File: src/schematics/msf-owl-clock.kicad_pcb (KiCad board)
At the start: 4 copper layers, 130.1 x 183.6 mm, 448 parts, among them Q101 NX6008NBKW, Q301 NX6008NBKW, Q501 NX6008NBKW, Q502 NX6008NBKW, Q503 NX6008NBKW, Q504 NX6008NBKW, Q505 NX6008NBKW, Q601 NX6008NBKW, Q602 BC847BS, Q603 BC847BS, U001 BC805M, U002 TSOP75338TT, U101 MP5016HGQH, U102 BQ24392RSER, U103 FUSB302BMPX, U104 TPS628512DRLR, U201 TPS7A2040PDQNR, U202 TPS7A2036PDBVR, U203 MCP6499, U204 MCP6499, U205 74HC595BQ, U206 TMUX1511RSV, U207 TMUX1511RSV, U301 PIC32CX1025SG41100-I/E5X, U302 AP22653AW6, U401 AP22653AW6, U402 MCP6486U, U403 IS31AP4991A-SLS2, U501 TPS7A2028PDBVR, U502 DPS310XTSA1, U503 HDC3022, U504 VL6180V1NR1, U601 TMUX1574RSV, U602 TMUX1574RSV, U603 TMUX1574RSV

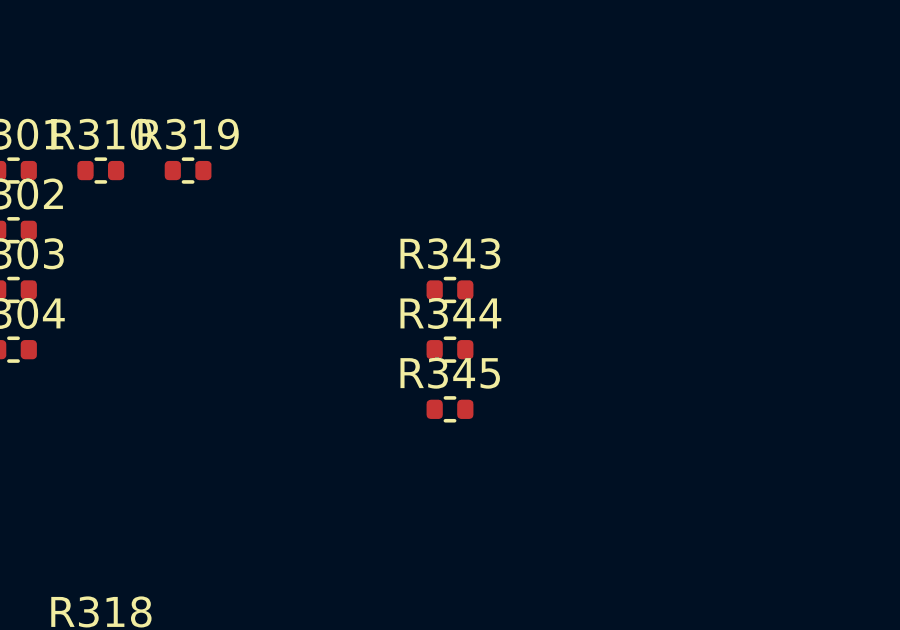
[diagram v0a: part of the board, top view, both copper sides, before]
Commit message: Updated reference designators after removing R320.
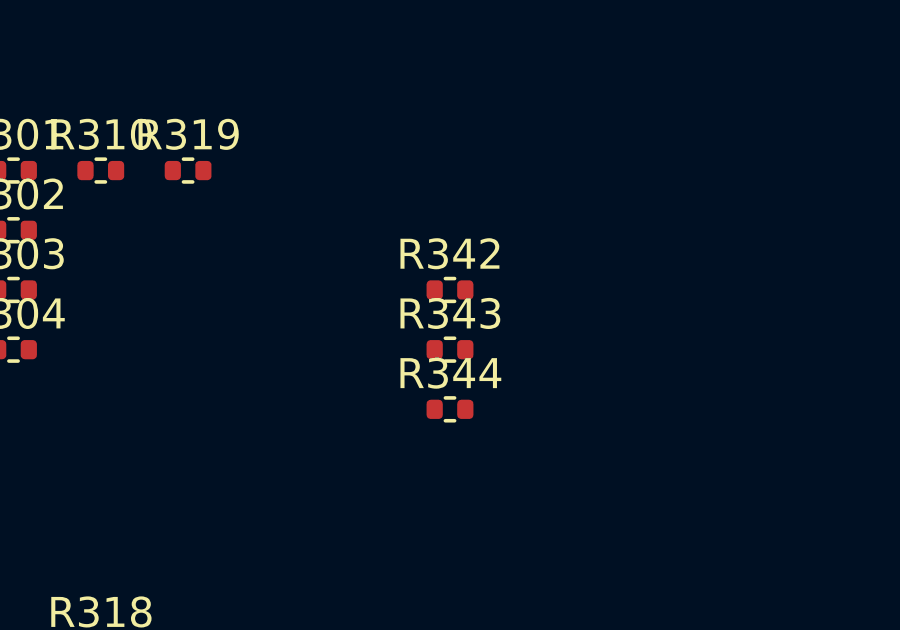
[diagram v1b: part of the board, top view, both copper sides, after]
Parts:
- renumbered R321 to R320, R322 to R321, R323 to R322, R324 to R323, R325 to R324, R326 to R325, R327 to R326, R328 to R327, R329 to R328, R330 to R329, R331 to R330, R332 to R331, R333 to R332, R334 to R333, R335 to R334, R336 to R335, R337 to R336, R338 to R337, R339 to R338, R340 to R339, R341 to R340, R342 to R341, R343 to R342, R344 to R343, R345 to R344, R346 to R345, R347 to R346
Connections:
- SPK001 pad MP: GND -> unconnected-(SPK001-PadMP)

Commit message: PCB routing.
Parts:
- removed NT201: Net Tie, restall-generic-wires:net-tie-2-6mil
- C227, C228, C229: moved to F.Cu
- C322: moved to B.Cu
- moved U502 225.4 mm to (189.7, 54.2)
- moved U503 225.4 mm to (201.1, 54.1)
- moved U504 225.4 mm to (190.1, 49.0)
- moved C322 198.0 mm to (100.8, 102.7), turned to -90 degrees
- moved C229 140.9 mm to (101.4, 102.8), turned to -90 degrees
- moved C228 126.4 mm to (89.0, 117.0), turned to 90 degrees
- moved TP301 123.0 mm to (184.2, 122.2), turned to 90 degrees
- moved C227 119.6 mm to (82.5, 125.9)
- moved C210 48.4 mm to (74.8, 132.2)
- moved C211 45.2 mm to (76.2, 128.4), turned to -90 degrees
- moved C209 40.7 mm to (76.2, 130.8), turned to 90 degrees
- moved C208 39.5 mm to (74.0, 133.7)
- moved U202 36.7 mm to (74.0, 129.6), turned to 90 degrees
- moved C212 32.0 mm to (74.0, 126.5)
- moved C233 7.52 mm to (68.0, 151.5), turned to -90 degrees
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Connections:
- ANT001 pad 2: /2-msf-receiver/MSF_ANT_{-} -> /2-msf-receiver/MSF_RCV_VREF_{+1.8V}
- C012 pad 2: /2-msf-receiver/MSF_ANT_{-} -> /2-msf-receiver/MSF_RCV_VREF_{+1.8V}
- C013 pad 2: /2-msf-receiver/MSF_ANT_{-} -> /2-msf-receiver/MSF_RCV_VREF_{+1.8V}
- C014 pad 2: /2-msf-receiver/MSF_ANT_{-} -> /2-msf-receiver/MSF_RCV_VREF_{+1.8V}
- C233 pad 1: /2-msf-receiver/MSF_ANT_{-} -> /2-msf-receiver/MSF_RCV_VREF_{+1.8V}
- U206 pad 12: GND -> (no net)
- U207 pad 12: GND -> (no net)
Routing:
- net /2-msf-receiver/MSF_ANT_{-}: track 87.3 -> 0.00 mm
- net /2-msf-receiver/MSF_RCV_VREF_{+1.8V}: track 23.9 -> 75.2 mm, vias 12 -> 14
- net /2-msf-receiver/MSF_ANT_{+}: track 76.6 -> 111.4 mm
- net /2-msf-receiver/2-msf-receiver-trf/PGA2.SW_EN3: track 44.4 -> 63.6 mm, vias 0 -> 2
- net /2-msf-receiver/2-msf-receiver-trf/PGA2.SW_EN0: track 42.6 -> 58.5 mm, vias 1 -> 2
- net /2-msf-receiver/2-msf-receiver-trf/PGA2.SW_EN1: track 41.7 -> 56.8 mm, vias 0 -> 2
- net Net-(C230-Pad1): track 0.00 -> 12.7 mm
- net /2-msf-receiver/2-msf-receiver-trf/PGA2.SW_EN2: track 49.1 -> 58.3 mm, vias 0 -> 2
- net /3-mcu-core/MCU_XOSC32K_IN: track 0.00 -> 5.63 mm
- net Net-(U201-OUT): track 0.00 -> 4.41 mm
- net Net-(C320-Pad1): track 0.00 -> 4.07 mm
- net /2-msf-receiver/2-msf-receiver-trf/PGA1.SW_EN1: track 7.80 -> 5.04 mm, vias 0 -> 1
- net /1-usb-and-power/~{CHARGER_DETECTED}: track 1.65 -> 3.96 mm, vias 0 -> 1
- net /1-usb-and-power/~{HAS_DATA}: track 1.47 -> 3.54 mm, vias 0 -> 1
- net /1-usb-and-power/~{CHARGING_ALLOWED}: track 1.23 -> 3.23 mm, vias 2 -> 3
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- added copper zone on F.Cu, net /1-usb-and-power/CORE_VDD_{+5V}
- added copper zone on B.Cu, net /2-msf-receiver/MSF_RCV_VREF_{+1.8V}
- added copper zone on F.Cu, net /2-msf-receiver/MSF_RCV_VREF_{+1.8V}
- added copper zone on F.Cu, net /2-msf-receiver/MSF_RCV_VREF_{+2.5V}
- added copper zone on F.Cu, net /2-msf-receiver/MSF_VDD_{+3.6V}
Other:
- board text added: "TODO: MSF +3.6V SHOULD HAVE CLEARANCE OF ABOUT 1mm TO THE +1.8V AND +2.5V REFERENCE FILLS"
- board text removed: "TODO: OPTIMISE TRF OUTPUT"

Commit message: PCB routing.
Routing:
- net Net-(U201-OUT): vias 2 -> 16
- net GND: vias 331 -> 329
- net /2-msf-receiver/MSF_VDD_{+3.6V}: vias 19 -> 24
- added copper zone on B.Cu, net Net-(U201-OUT)
- added copper zone on F.Cu, net Net-(U201-OUT)
